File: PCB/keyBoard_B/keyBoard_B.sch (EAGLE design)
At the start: 597 parts, among them IC1 MEGA8-AI, J1 J, J10 J, J11 J, J12 J, J13 J, J14 J, J15 J, J16 J, J17 J, J2 J, J3 J, J4 J, J5 J, J6 J, J7 J, J8 J, J9 J

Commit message: move +m2
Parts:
- removed D100, D101, D102, D103, D104, D105, D106, D107, D108, D109, D110, D87, D88, D89, D90, D91, D92, D93, D94, D95, D96, D97, D98, D99: LL4148, detali:LL4148
- removed HL4: (no value), led:RGB2X5
- removed IC1: MEGA8-AI, atmel:MEGA8-AI
- removed JA100, JA101, JA102, JA103, JA104, JA105, JA106, JA107, JA108, JA109, JA110, JA87, JA88, JA89, JA90, JA91, JA92, JA93, JA94, JA95, JA96, JA97, JA98, JA99, JB100, JB101, JB102, JB103, JB104, JB105, JB106, JB107, JB108, JB109, JB110, JB87, JB88, JB89, JB90, JB91, JB92, JB93, JB94, JB95, JB96, JB97, JB98, JB99: (no value), detali:SJ
- removed S100: 4, cherrymx:CHERRY-MX-4P
- removed S101: 5, cherrymx:CHERRY-MX-4P
- removed S102: 6, cherrymx:CHERRY-MX-4P
- removed S103: +, cherrymx:CHERRY-MX-4P
- removed S104: 1, cherrymx:CHERRY-MX-4P
- removed S105: 2, cherrymx:CHERRY-MX-4P
- removed S106: 3, cherrymx:CHERRY-MX-4P
- removed S107: NumEnter, cherrymx:CHERRY-MX-4P
- removed S107B: NumEnter, cherrymx:CHERRY-MX
- removed S108: 0, cherrymx:CHERRY-MX-4P
- removed S109: 00, cherrymx:CHERRY-MX-4P
- removed S110: ., cherrymx:CHERRY-MX-4P
- removed S67B: |, cherrymx:CHERRY-MX
- removed S74B: Enter, cherrymx:CHERRY-MX
- removed S87: Num, cherrymx:CHERRY-MX-4P
- removed S88: D, cherrymx:CHERRY-MX-4P
- removed S89: E, cherrymx:CHERRY-MX-4P
- removed S90: F, cherrymx:CHERRY-MX-4P
- removed S91: /, cherrymx:CHERRY-MX-4P
- removed S92: A, cherrymx:CHERRY-MX-4P
- removed S93: B, cherrymx:CHERRY-MX-4P
- removed S94: C, cherrymx:CHERRY-MX-4P
- removed S95: *, cherrymx:CHERRY-MX-4P
- removed S96: 7, cherrymx:CHERRY-MX-4P
- removed S97: 8, cherrymx:CHERRY-MX-4P
- removed S98: 9, cherrymx:CHERRY-MX-4P
- removed S99: -, cherrymx:CHERRY-MX-4P
- removed SV2: (no value), con-lsta:FE06-1
- removed SV3: (no value), con-lsta:FE07-1
- added 3D3: 74AC138N, detali2:74AC138N
- added JA67B, JB67B: (no value), detali:SJ
- S47, S48, S49, S50, S51, S52, S53, S54, S55, S56, S57, S58, S59, S60, S61, S62, S63, S64, S65, S66, S67, S67C, S68, S69, S70, S71, S72, S73, S74, S74A, S75, S76, S77, S78, S79, S80, S81, S82, S83, S84, S85, S86: device cherrymx:CHERRY-MX -> cherrymx:CHERRY-MX-4P
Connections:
- removed net 3A1: JA103.2, JA89.2, JA96.2, JA97.2, JA98.2, SV2.1
- removed net 3A2: JA100.2, JA101.2, JA102.2, SV2.2
- removed net 3A3: JA104.2, JA105.2, JA106.2, JA107.2, JA88.2, JA90.2, JA92.2, SV2.3
- removed net 3A4: JA108.2, JA110.2, SV2.4
- removed net 3A5: JA87.2, JA91.2, JA94.2, JA95.2, SV2.5
- removed net 3A6: JA93.2, JA99.2, SV2.6
- removed net 3B0: D92.C, SV3.1
- removed net 3B10: D100.C, D104.C, D87.C, D96.C, SV3.7
- removed net 3B2: D88.C, D89.C, D94.C, SV3.2
- removed net 3B3: D90.C, D93.C, SV3.3
- removed net 3B7: D103.C, D107.C, SV3.4
- removed net 3B8: D102.C, D106.C, D110.C, D95.C, D98.C, D99.C, SV3.5
- removed net 3B9: D101.C, D105.C, D108.C, D91.C, D97.C, SV3.6
- removed net N$269: D88.A, JB88.1
- removed net N$270: JB87.2, S87G$1.PIN-1
- removed net N$271: JB88.2, S88G$1.PIN-1
- removed net N$272: JA87.1, S87G$1.PIN-2
- removed net N$273: JA88.1, S88G$1.PIN-2
- removed net N$274: D89.A, JB89.1
- removed net N$275: JB89.2, S89G$1.PIN-1
- removed net N$276: JA89.1, S89G$1.PIN-2
- removed net N$277: D90.A, JB90.1
- removed net N$278: JB90.2, S90G$1.PIN-1
- removed net N$279: JA90.1, S90G$1.PIN-2
- removed net N$280: D91.A, JB91.1
- removed net N$281: JB91.2, S91G$1.PIN-1
- removed net N$282: JA91.1, S91G$1.PIN-2
- removed net N$283: JB92.2, S92G$1.PIN-1
- removed net N$284: D92.A, JB92.1
- removed net N$285: JA92.1, S92G$1.PIN-2
- removed net N$286: JA93.1, S93G$1.PIN-2
- removed net N$287: JB93.2, S93G$1.PIN-1
- removed net N$288: D93.A, JB93.1
- removed net N$289: D94.A, JB94.1
- removed net N$290: JB94.2, S94G$1.PIN-1
- removed net N$291: JA94.1, S94G$1.PIN-2
- removed net N$292: D95.A, JB95.1
- removed net N$293: JB95.2, S95G$1.PIN-1
- removed net N$294: JA95.1, S95G$1.PIN-2
- removed net N$295: D96.A, JB96.1
- removed net N$296: JB96.2, S96G$1.PIN-1
- removed net N$297: JA96.1, S96G$1.PIN-2
- removed net N$298: JB97.2, S97G$1.PIN-1
- removed net N$299: JA97.1, S97G$1.PIN-2
- removed net N$300: D97.A, JB97.1
- removed net N$301: D98.A, JB98.1
- removed net N$302: JB98.2, S98G$1.PIN-1
- removed net N$303: JA98.1, S98G$1.PIN-2
- removed net N$304: D99.A, JB99.1
- removed net N$305: JB99.2, S99G$1.PIN-1
- removed net N$306: JA99.1, S99G$1.PIN-2
- removed net N$307: D100.A, JB100.1
- removed net N$308: JB100.2, S100G$1.PIN-1
- removed net N$309: JA100.1, S100G$1.PIN-2
- removed net N$310: JB101.2, S101G$1.PIN-1
- removed net N$311: D101.A, JB101.1
- removed net N$312: JA101.1, S101G$1.PIN-2
- removed net N$313: D102.A, JB102.1
- removed net N$314: JB102.2, S102G$1.PIN-1
- removed net N$315: JA102.1, S102G$1.PIN-2
- removed net N$316: D103.A, JB103.1
- removed net N$317: JB103.2, S103G$1.PIN-1
- removed net N$318: JA103.1, S103G$1.PIN-2
- removed net N$319: JB107.2, S107B.PIN-1, S107G$1.PIN-1
- removed net N$320: JB104.2, S104G$1.PIN-1
- removed net N$321: JA104.1, S104G$1.PIN-2
- removed net N$322: JB105.2, S105G$1.PIN-1
- removed net N$323: D105.A, JB105.1
- removed net N$324: JA105.1, S105G$1.PIN-2
- removed net N$325: D106.A, JB106.1
- removed net N$326: JB106.2, S106G$1.PIN-1
- removed net N$327: JA106.1, S106G$1.PIN-2
- removed net N$328: D107.A, JB107.1
- removed net N$329: JB108.2, S108G$1.PIN-1
- removed net N$330: JA108.1, S108G$1.PIN-2
- removed net N$331: D108.A, JB108.1
- removed net N$332: JB109.2, S109G$1.PIN-1
- removed net N$333: D109.A, JB109.1
- removed net N$334: JA109.1, S109G$1.PIN-2
- removed net N$335: D110.A, JB110.1
- removed net N$336: JB110.2, S110G$1.PIN-1
- removed net N$337: JA110.1, S110G$1.PIN-2
- net N$112: now also S47G$1.PIN-1; no longer S47.PIN-1
- net N$127: now also S53G$1.PIN-1; no longer S53.PIN-1
- net N$153: now also S60G$1.PIN-1; no longer S60.PIN-1
- net N$154: now also S68G$1.PIN-1; no longer S68.PIN-1
- net N$155: now also S75G$1.PIN-1; no longer S75.PIN-1
- net N$156: now also S82G$1.PIN-1; no longer S82.PIN-1
- net N$157: now also S48G$1.PIN-1; no longer S48.PIN-1
- net N$158: now also S54G$1.PIN-1; no longer S54.PIN-1
- net N$159: now also S61G$1.PIN-1; no longer S61.PIN-1
- net N$160: now also S69G$1.PIN-1; no longer S69.PIN-1
- net N$161: now also S76G$1.PIN-1; no longer S76.PIN-1
- net N$162: now also S83G$1.PIN-1; no longer S83.PIN-1
- net N$163: now also S49G$1.PIN-1; no longer S49.PIN-1
- net N$164: now also S55G$1.PIN-1; no longer S55.PIN-1
- net N$165: now also S62G$1.PIN-1; no longer S62.PIN-1
- net N$166: now also S70G$1.PIN-1; no longer S70.PIN-1
- net N$167: now also S77G$1.PIN-1; no longer S77.PIN-1
- net N$168: now also S84G$1.PIN-1; no longer S84.PIN-1
- net N$169: now also S50G$1.PIN-1; no longer S50.PIN-1
- net N$170: now also S56G$1.PIN-1; no longer S56.PIN-1
- net N$171: now also S71G$1.PIN-1; no longer S71.PIN-1
- net N$172: now also S78G$1.PIN-1; no longer S78.PIN-1
- net N$173: now also S85G$1.PIN-1; no longer S85.PIN-1
- net N$174: now also S51G$1.PIN-1; no longer S51.PIN-1
- net N$175: now also S57G$1.PIN-1; no longer S57.PIN-1
- net N$176: now also S64G$1.PIN-1; no longer S64.PIN-1
- net N$177: now also S72G$1.PIN-1; no longer S72.PIN-1
- net N$178: now also S79G$1.PIN-1; no longer S79.PIN-1
- net N$179: now also S86G$1.PIN-1; no longer S86.PIN-1
- net N$180: now also S58G$1.PIN-1; no longer S58.PIN-1
- net N$181: now also S65G$1.PIN-1; no longer S65.PIN-1
- net N$182: now also S80G$1.PIN-1; no longer S80.PIN-1
- net N$183: now also S59G$1.PIN-1; no longer S59.PIN-1
- net N$184: now also S66G$1.PIN-1; no longer S66.PIN-1
- net N$185: now also S67G$1.PIN-1; no longer S67.PIN-1, S67B.PIN-1, S67C.PIN-2
- net N$186: now also S81G$1.PIN-1; no longer S81.PIN-1
- net N$224: now also JB67B.1
- net N$227: now also S66G$1.PIN-2; no longer S66.PIN-2
- net N$228: now also S47G$1.PIN-2; no longer S47.PIN-2
- net N$229: now also S53G$1.PIN-2; no longer S53.PIN-2
- net N$230: now also S60G$1.PIN-2; no longer S60.PIN-2
- net N$231: now also S68G$1.PIN-2; no longer S68.PIN-2
- net N$232: now also S75G$1.PIN-2; no longer S75.PIN-2
- net N$233: now also S82G$1.PIN-2; no longer S82.PIN-2
- net N$234: now also S48G$1.PIN-2; no longer S48.PIN-2
- net N$235: now also S54G$1.PIN-2; no longer S54.PIN-2
- net N$236: now also S61G$1.PIN-2; no longer S61.PIN-2
- net N$237: now also S69G$1.PIN-2; no longer S69.PIN-2
- net N$238: now also S76G$1.PIN-2; no longer S76.PIN-2
- net N$239: now also S83G$1.PIN-2; no longer S83.PIN-2
- net N$240: now also S49G$1.PIN-2; no longer S49.PIN-2
- net N$241: now also S55G$1.PIN-2; no longer S55.PIN-2
- net N$242: now also S62G$1.PIN-2; no longer S62.PIN-2
- net N$243: now also S70G$1.PIN-2; no longer S70.PIN-2
- net N$244: now also S77G$1.PIN-2; no longer S77.PIN-2
- net N$245: now also S84G$1.PIN-2; no longer S84.PIN-2
- net N$246: now also S50G$1.PIN-2; no longer S50.PIN-2
- net N$247: now also S56G$1.PIN-2; no longer S56.PIN-2
- net N$248: now also S63G$1.PIN-2; no longer S63.PIN-2
- net N$249: now also S71G$1.PIN-2; no longer S71.PIN-2
- net N$250: now also S78G$1.PIN-2; no longer S78.PIN-2
- net N$251: now also S85G$1.PIN-2; no longer S85.PIN-2
- net N$252: now also S51G$1.PIN-2; no longer S51.PIN-2
- net N$253: now also S57G$1.PIN-2; no longer S57.PIN-2
- net N$254: now also S64G$1.PIN-2; no longer S64.PIN-2
- net N$255: now also S72G$1.PIN-2; no longer S72.PIN-2
- net N$256: now also S79G$1.PIN-2; no longer S79.PIN-2
- net N$257: now also S86G$1.PIN-2; no longer S86.PIN-2
- net N$258: now also S52G$1.PIN-2; no longer S52.PIN-2
- net N$259: now also S58G$1.PIN-2; no longer S58.PIN-2
- net N$260: now also S65G$1.PIN-2; no longer S65.PIN-2
- net N$261: now also S73G$1.PIN-2; no longer S73.PIN-2
- net N$262: now also S80G$1.PIN-2; no longer S80.PIN-2
- net N$263: now also S81G$1.PIN-2; no longer S81.PIN-2
- net N$264: now also S67G$1.PIN-2; no longer S67.PIN-2, S67B.PIN-2, S67C.PIN-1
- net N$265: now also S59G$1.PIN-2; no longer S59.PIN-2
- net N$267: now also S74G$1.PIN-2; no longer S74.PIN-2
- net N$268: now also JA67.2, JA67B.2; no longer D87.A, JB87.1
- net N$51: now also JB67B.2, S67CG$1.PIN-2; no longer JA107.1, S107B.PIN-2, S107G$1.PIN-2
- net N$60: now also JA67B.1, S67CG$1.PIN-1; no longer D104.A, JB104.1
- net N$70: now also S74G$1.PIN-1; no longer S74.PIN-1
- net N$71: now also S52G$1.PIN-1; no longer S52.PIN-1
- net N$84: now also S63G$1.PIN-1; no longer S63.PIN-1
- net N$89: now also S73G$1.PIN-1; no longer S73.PIN-1
- net N$94: now also S74AG$1.PIN-1; no longer S74A.PIN-1, S74B.PIN-1
- net N$97: now also S74AG$1.PIN-2; no longer S74A.PIN-2, S74B.PIN-2
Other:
- moved on the sheet: D67, S67C

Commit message: .
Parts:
- removed 2S1: (no value), con-lsta:FE10-1
- removed 2S2, 2S3: (no value), con-lsta:FE08-1
- removed 2S4: (no value), con-lsta:FE05-1
- removed R3: 1k, rcl:R-EU_R0805
- added S67C1: |, cherrymx:CHERRY-MX-4P
- added U$88: CHERRY-MX, cherrymx:CHERRY-MX
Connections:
- removed net 2A2: 2S3.2, JA47.2, JA60.2
- removed net 2A4: 2S3.4, JA68.2, JA82.2
- removed net 2B0: 2S1.1, D53.C
- removed net 2B1: 2S1.2, D54.C
- removed net 2B10: 2S2.1, D82.C
- removed net 2B4: 2S1.5, D60.C, D61.C, D68.C, D69.C, D75.C, D76.C
- removed net 2B6: 2S1.7, D47.C, D48.C, D83.C
- removed net GND_K2: R3.1
- removed net N$152: R3.2
- net 2A6: no longer 2S3.6, JA75.2
- net 2A7: no longer 2S3.7
- net 2A8: no longer 2S3.8, JA53.2
- net N$94: now also U$88.PIN-1
- net N$97: now also U$88.PIN-2
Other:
- moved on the sheet: D64B, JA59, JA66, JA67, JA67B, JA74B, JB74B, S59, S66, S67, S67C, S74

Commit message: arc
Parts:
- added IC1: 74ALS04N, detali2:74ALS04N
- added S67C2: FN1, cherrymx:CHERRY-MX-4P
- S67C1: value | -> FN2
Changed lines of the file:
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@@
 <part name="JB67B" library="detali" deviceset="SJ" device=""/>
 <part name="U$88" library="cherrymx" deviceset="CHERRY-MX" device=""/>
-<part name="S67C1" library="cherrymx" deviceset="CHERRY-MX-4P" device="" value="|"/>
+<part name="S67C1" library="cherrymx" deviceset="CHERRY-MX-4P" device="" value="FN2"/>
+<part name="IC1" library="detali2" deviceset="74*04" device="N" technology="ALS"/>
+<part name="S67C2" library="cherrymx" deviceset="CHERRY-MX-4P" device="" value="FN1"/>
 </parts>
 <sheets>
@@
 <instance part="U$88" gate="G$1" x="480.06" y="-7.62"/>
 <instance part="S67C1" gate="G$1" x="414.02" y="-2.54" rot="MR0"/>
+<instance part="IC1" gate="A" x="322.58" y="-73.66"/>
+<instance part="S67C2" gate="G$1" x="363.22" y="-5.08" rot="MR0"/>
 </instances>
 <busses>

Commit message: get all vil
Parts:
- removed 1S1, 1S1O: (no value), con-lsta:FE10-1
- removed 1S2, 1S2O, 1S3, 1S3O: (no value), con-lsta:FE08-1
- removed 1S4, 1S4O: (no value), con-lsta:FE05-1
- removed 3D1: 74HC138N, detali:74HC138N
- removed 3D2: К155ЛА4, detali:74HC10N
- removed 3D3: 74AC138N, detali2:74AC138N
- removed D10, D11, D111, D112, D113, D114, D115, D116, D117, D118, D119, D12, D120, D121, D122, D123, D124, D125, D126, D127, D128, D129, D13, D130, D131, D132, D133, D134, D135, D136, D14, D15, D16, D17, D18, D19, D20, D21, D22, D23, D24, D25, D26, D27, D28, D29, D3, D30, D31, D32, D33, D34, D35, D36, D37, D38, D39, D4, D40, D41, D42, D43, D44, D45, D46, D5, D6, D7, D8, D9: LL4148, detali:LL4148
- removed HL1, HL2, HL3: (no value), led:RGB2X5
- removed IC1: 74ALS04N, detali2:74ALS04N
- removed J13: J, detali:J
- removed JA1, JA10, JA11, JA12, JA2, JA3, JA4, JA5, JA6, JA7, JA8, JA9, JB10, JB11, JB12, JB13, JB14, JB15, JB16, JB17, JB2, JB4, JB5, JB6, JB7, JB8, JB9: (no value), jumper:SJ
- removed JA111, JA112, JA113, JA114, JA115, JA116, JA117, JA118, JA119, JA120, JA121, JA122, JA123, JA124, JA125, JA126, JA127, JA128, JA129, JA13, JA130, JA131, JA132, JA133, JA14, JA15, JA16, JA17, JA18, JA19, JA20, JA21, JA22, JA23, JA24, JA25, JA26, JA27, JA28, JA29, JA30, JA31, JA32, JA33, JA34, JA35, JA36, JA37, JA38, JA39, JA40, JA41, JA42, JA43, JA44, JA45, JA46, JB1, JB111, JB112, JB113, JB114, JB115, JB116, JB117, JB118, JB119, JB120, JB121, JB122, JB123, JB124, JB125, JB126, JB127, JB128, JB129, JB130, JB131, JB132, JB133, JB18, JB19, JB20, JB21, JB22, JB23, JB24, JB25, JB26, JB27, JB28, JB29, JB3, JB30, JB31, JB32, JB33, JB34, JB35, JB36, JB37, JB38, JB39, JB40, JB41, JB42, JB43, JB44, JB45, JB46, JB67B: (no value), detali:SJ
- removed LED1: (no value), detali:LED5MM
- removed R1, R2: 1k, rcl:R-EU_R1206W
- removed R4, R5, R6: 10k, rcl:R-EU_R1206W
- removed R7, R8: (no value), rcl:R-EU_R1206W
- removed S1: Scroll Lock, cherrymx:CHERRY-MX-LED
- removed S10: Left, cherrymx:CHERRY-MX
- removed S107B1, S130: NumEnter, cherrymx:CHERRY-MX-4P
- removed S11: Down, cherrymx:CHERRY-MX
- removed S111: D, cherrymx:CHERRY-MX-4P
- removed S112: E, cherrymx:CHERRY-MX-4P
- removed S113: F, cherrymx:CHERRY-MX-4P
- removed S114: /, cherrymx:CHERRY-MX-4P
- removed S115: A, cherrymx:CHERRY-MX-4P
- removed S116: B, cherrymx:CHERRY-MX-4P
- removed S117: C, cherrymx:CHERRY-MX-4P
- removed S118: *, cherrymx:CHERRY-MX-4P
- removed S119: 7, cherrymx:CHERRY-MX-4P
- removed S12: Right, cherrymx:CHERRY-MX
- removed S120: 8, cherrymx:CHERRY-MX-4P
- removed S121: 9, cherrymx:CHERRY-MX-4P
- removed S122: -, cherrymx:CHERRY-MX-4P
- removed S123: 4, cherrymx:CHERRY-MX-4P
- removed S124: 5, cherrymx:CHERRY-MX-4P
- removed S125: 6, cherrymx:CHERRY-MX-4P
- removed S126: +, cherrymx:CHERRY-MX-4P
- removed S127: 1, cherrymx:CHERRY-MX-4P
- removed S128: 2, cherrymx:CHERRY-MX-4P
- removed S129: 3, cherrymx:CHERRY-MX-4P
- removed S13: F1, cherrymx:CHERRY-MX
- removed S131: 0, cherrymx:CHERRY-MX-4P
- removed S132: 00, cherrymx:CHERRY-MX-4P
- removed S133: ., cherrymx:CHERRY-MX-4P
- removed S134: NumLock, detali:31-XX
- removed S14: F2, cherrymx:CHERRY-MX
- removed S15: F3, cherrymx:CHERRY-MX
- removed S16: F4, cherrymx:CHERRY-MX
- removed S17: F5, cherrymx:CHERRY-MX
- removed S18: F6, cherrymx:CHERRY-MX
- removed S19: 1, cherrymx:CHERRY-MX
- removed S2: ESC, cherrymx:CHERRY-MX-LED
- removed S20: 2, cherrymx:CHERRY-MX
- removed S21: 3, cherrymx:CHERRY-MX
- removed S22: 4, cherrymx:CHERRY-MX
- removed S23: 5, cherrymx:CHERRY-MX
- removed S24: 6, cherrymx:CHERRY-MX
- removed S25: TAB, cherrymx:CHERRY-MX
- removed S26: Q, cherrymx:CHERRY-MX
- removed S27: W, cherrymx:CHERRY_MX
- removed S28: E, cherrymx:CHERRY-MX
- removed S29: R, cherrymx:CHERRY-MX
- removed S3: Ins, cherrymx:CHERRY-MX-LED
- removed S30: T, cherrymx:CHERRY-MX
- removed S31: LCtrl, cherrymx:CHERRY-MX
- removed S32: A, cherrymx:CHERRY-MX
- removed S33: S, cherrymx:CHERRY-MX
- removed S34: D, cherrymx:CHERRY-MX
- removed S35: F, cherrymx:CHERRY-MX
- removed S36: G, cherrymx:CHERRY-MX
- removed S37, S37B, S37B1: L Shift, cherrymx:CHERRY-MX
- removed S38: Z, cherrymx:CHERRY-MX
- removed S39: X, cherrymx:CHERRY-MX
- removed S4: Pause, cherrymx:CHERRY_MX
- removed S40: C, cherrymx:CHERRY-MX
- removed S41: V, cherrymx:CHERRY-MX
- removed S42: B, cherrymx:CHERRY-MX
- removed S43: Caps Lock, cherrymx:CHERRY-MX-LED
- removed S44: Alt, cherrymx:CHERRY-MX
- removed S45: Menu(Win), cherrymx:CHERRY-MX
- removed S46: Space, cherrymx:CHERRY-MX
- removed S5: Home, cherrymx:CHERRY-MX
- removed S6: P Up, cherrymx:CHERRY-MX
- removed S67C2: FN1, cherrymx:CHERRY-MX-4P
- removed S7: End, cherrymx:CHERRY-MX
- removed S8: P Dn, cherrymx:CHERRY-MX
- removed S9: Up, cherrymx:CHERRY-MX
- removed U$88: CHERRY-MX, cherrymx:CHERRY-MX
- added 2D1: 74HC138N, detali2:74AC138N
- added 2D2: 74HC04N, detali2:74ALS04N
- added D67B, D87: LL4148, detali:LL4148
- added J18, J19, J21, J22, J23, J24, J25, J26, J27, J28, J29, J30, J31, J32, J33, J34, J35, J36, J37, J38, J39, J40, J41, J42, J43, J44, J46, J48, J49, J50, J51, J52, J53: J, detali2:J
- added JA67B1, JA87, JB67B1, JB87: (no value), detali:SJ
- added R3: 1k, rcl:R-EU_R0805
- added S67B: |u, cherrymx:CHERRY-MX
- added S74B: Enter, cherrymx:CHERRY-MX
- C1: value (none) -> 100n; device rcl:C-EUC1206 -> rcl:C-EUC0805
- C2: value (none) -> 100n
- J1, J10, J11, J12, J14, J15, J16, J17, J2, J3, J4, J5, J6, J7, J8, J9: device detali:J -> detali2:J
- S67: value | -> |d
- S83: value Mouse2(Menu) -> FN3
- S84: value Alt -> R_Alt
- SV1: value (none) -> CON_KB_B; device detali:FE09-1 -> detali2:FE12-1
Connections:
- removed net +5V_K1: 1S4.4, R1.1, R2.1
- removed net 2A1: JA61.2
- removed net 2A3: JA69.2
- removed net 2A5: JA76.2
- removed net 2A6: JA83.2
- removed net 2A7: JA48.2
- removed net 2A8: JA54.2
- removed net A1: 1S3.1, JA1.2, JA26.2, JA28.2, JA29.2
- removed net A2: 1S3.2, 1S3O.2, JA15.2, JA25.2, JA30.2, JA37.2, JA43.2, JA45.2
- removed net A3: 1S3.3, JA27.2, JA32.2, JA33.2, JA34.2, JA35.2
- removed net A4: 1S3.4, JA16.2, JA18.2, JA2.2, JA36.2, JA44.2, JA46.2, JA9.2
- removed net A5: 1S3.5, JA38.2, JA39.2, JA40.2, JA41.2
- removed net A6: 1S3.6, JA10.2, JA11.2, JA12.2, JA42.2
- removed net A7: 1S3.7, D24.A, JA13.2, JA14.2, JA23.2, JA3.2, JA31.2, JA5.2, JA6.2
- removed net A8: 1S3.8, JA17.2, JA19.2, JA20.2, JA21.2, JA22.2, JA4.2, JA7.2, JA8.2
- removed net B0: 1S1.1, D2.C, D25.C, D26.C, D32.C, D38.C
- removed net B1: 1S1.2, D13.C, D33.C, D39.C, D43.C, HL1.AB, HL2.AB
- removed net B10: 1S2.1, D11.C, D46.C
- removed net B11: 1S2.2, D37.C
- removed net B12: 1S2.3
- removed net B13: 1S2.4, D22.C
- removed net B14: 1S2.5, D1.C, D27.C, D4.C, D44.C
- removed net B15: 1S2.6, D17.C, D31.C
- removed net B16: 1S2.7, D45.C
- removed net B17: 1S2.8
- removed net B2: 1S1.3, D14.C, D15.C, D16.C, D28.C, D34.C, D40.C, HL3.AB
- removed net B3: 1S1.4, D23.C, D29.C, D30.C, D35.C, D36.C, D41.C, D42.C
- removed net B4: 1S1.5, D19.C, JA24.2
- removed net B5: 1S1.6, D18.C, D20.C
- removed net B6: 1S1.7, 1S2O.5, D21.C
- removed net B7: 1S1.8, D10.C, D5.C, D7.C, D9.C
- removed net B8: 1S1.9, D6.C, D8.C
- removed net B9: 1S1.10, D12.C, D3.C
- removed net COLN1: 3D2A.O, SV1.2
- removed net COLN2: 3D2B.O, J15.P$1
- removed net COLN3: 3D2C.O, SV1.3
- removed net GND_K1: 1S4.5
- removed net K1: HL1.C, HL3.C
- removed net LED_CAPS: 1S4.3, S43_LED.LED2
- removed net LED_NUM: 1S4.1
- removed net LED_SCR: 1S4.2, S1_LED.LED2
- removed net N$100: JA30.1, S30.PIN-2
- removed net N$101: JA31.1, S31.PIN-2
- removed net N$102: JA32.1, S32.PIN-2
- removed net N$103: JA33.1, S33.PIN-2
- removed net N$104: JA34.1, S34.PIN-2
- removed net N$105: JA35.1, S35.PIN-2
- removed net N$106: JA36.1, S36.PIN-2
- removed net N$107: JA37.1, S37.PIN-2, S37B.PIN-2, S37B1.PIN-2
- removed net N$108: JA38.1, S38.PIN-2
- removed net N$109: JA39.1, S39.PIN-2
- removed net N$110: JA40.1, S40.PIN-2
- removed net N$111: JA41.1, S41.PIN-2
- removed net N$113: JA43.1, S43G$1.PIN-2
- removed net N$114: JA45.1, S45.PIN-2
- removed net N$115: JA46.1, S46.PIN-2
- removed net N$116: JA19.1, S19.PIN-2
- removed net N$117: JA44.1, S44.PIN-2
- removed net N$118: JA21.1, S21.PIN-2
- removed net N$119: JA16.1, S16.PIN-2
- removed net N$120: D17.A, JB17.1
- removed net N$121: D18.A, JB18.1
- removed net N$122: D19.A, JB19.1
- removed net N$123: D20.A, JB20.1
- removed net N$124: D21.A, JB21.1
- removed net N$125: D22.A, JB22.1
- removed net N$126: D23.A, JB23.1
- removed net N$128: D25.A, JB25.1
- removed net N$129: D26.A, JB26.1
- removed net N$130: D27.A, JB27.1
- removed net N$131: D28.A, JB28.1
- removed net N$132: D29.A, JB29.1
- removed net N$133: D30.A, JB30.1
- removed net N$134: D31.A, JB31.1
- removed net N$135: D32.A, JB32.1
- removed net N$136: D33.A, JB33.1
- removed net N$137: D34.A, JB34.1
- removed net N$138: D35.A, JB35.1
- removed net N$139: D36.A, JB36.1
- removed net N$140: D37.A, JB37.1
- removed net N$141: D38.A, JB38.1
- removed net N$142: D39.A, JB39.1
- removed net N$143: D40.A, JB40.1
- removed net N$144: D41.A, JB41.1
- removed net N$145: D42.A, JB42.1
- removed net N$146: D43.A, JB43.1
- removed net N$147: D44.A, JB44.1
- removed net N$148: D45.A, JB45.1
- removed net N$149: D46.A, JB46.1
- removed net N$150: R1.2, S1_LED.LED1
- removed net N$151: R2.2, S43_LED.LED1
- removed net N$28 (its old number): JA10.1, S10.PIN-2
- removed net N$29 (its old number): JA1.1, S1G$1.PIN-2
- removed net N$30: D9.A, JB9.1
- removed net N$31: D11.A, JB11.1
- removed net N$338: D112.A, S134.P
- removed net N$339: JA111.1, S111G$1.PIN-2
- removed net N$340: D113.A, JB112.1
- removed net N$341: JB112.2, S112G$1.PIN-1
- removed net N$342: JA112.1, S112G$1.PIN-2
- removed net N$343: D111.A, JB111.1
- removed net N$344: JB111.2, S111G$1.PIN-1
- removed net N$345: D114.A, JB113.1
- removed net N$346: JB113.2, S113G$1.PIN-1
- removed net N$347: JA113.1, S113G$1.PIN-2
- removed net N$348: D115.A, JB114.1
- removed net N$349: JB114.2, S114G$1.PIN-1
- removed net N$350: JA114.1, S114G$1.PIN-2
- removed net N$351: JB115.2, S115G$1.PIN-1
- removed net N$352: D116.A, JB115.1
- removed net N$353: JA115.1, S115G$1.PIN-2
- removed net N$354: JA116.1, S116G$1.PIN-2
- removed net N$355: JB116.2, S116G$1.PIN-1
- removed net N$356: D117.A, JB116.1
- removed net N$357: D118.A, JB117.1
- removed net N$358: JB117.2, S117G$1.PIN-1
- removed net N$359: JA117.1, S117G$1.PIN-2
- removed net N$360: D119.A, JB118.1
- removed net N$361: JB118.2, S118G$1.PIN-1
- removed net N$362: JA118.1, S118G$1.PIN-2
- removed net N$363: D120.A, JB119.1
- removed net N$364: JB119.2, S119G$1.PIN-1
- removed net N$365: JA119.1, S119G$1.PIN-2
- removed net N$366: JB120.2, S120G$1.PIN-1
- removed net N$367: JA120.1, S120G$1.PIN-2
- removed net N$368: D121.A, JB120.1
- removed net N$369: D122.A, JB121.1
- removed net N$370: JB121.2, S121G$1.PIN-1
- removed net N$371: JA121.1, S121G$1.PIN-2
- removed net N$372: D123.A, JB122.1
- removed net N$373: JB122.2, S122G$1.PIN-1
- removed net N$374: JA122.1, S122G$1.PIN-2
- removed net N$375: D124.A, JB123.1
- removed net N$376: JB123.2, S123G$1.PIN-1
- removed net N$377: JA123.1, S123G$1.PIN-2
- removed net N$378: JB124.2, S124G$1.PIN-1
- removed net N$379: D125.A, JB124.1
- removed net N$38: JA14.1, S14.PIN-2
- removed net N$380: JA124.1, S124G$1.PIN-2
- removed net N$381: D126.A, JB125.1
- removed net N$382: JB125.2, S125G$1.PIN-1
- removed net N$383: JA125.1, S125G$1.PIN-2
- removed net N$384: D127.A, JB126.1
- removed net N$385: JB126.2, S126G$1.PIN-1
- removed net N$386: JA126.1, S126G$1.PIN-2
- removed net N$387: JB130.2, S107B1G$1.PIN-1, S130G$1.PIN-1
- removed net N$388: JA130.1, S107B1G$1.PIN-2, S130G$1.PIN-2
- removed net N$389: D128.A, JB127.1
- removed net N$390: JB127.2, S127G$1.PIN-1
- removed net N$391: JA127.1, S127G$1.PIN-2
- removed net N$392: JB128.2, S128G$1.PIN-1
- removed net N$393: D129.A, JB128.1
- removed net N$394: JA128.1, S128G$1.PIN-2
- removed net N$395: D130.A, JB129.1
- removed net N$396: JB129.2, S129G$1.PIN-1
- removed net N$397: JA129.1, S129G$1.PIN-2
- removed net N$398: JB131.2, S131G$1.PIN-1
- removed net N$399: JA131.1, S131G$1.PIN-2
- removed net N$40: JA13.1, S13.PIN-2
- removed net N$400: D132.A, JB131.1
- removed net N$401: JB132.2, S132G$1.PIN-1
- removed net N$402: D133.A, JB132.1
- removed net N$403: JA132.1, S132G$1.PIN-2
- removed net N$404: D134.A, JB133.1
- removed net N$405: JB133.2, S133G$1.PIN-1
- removed net N$406: JA133.1, S133G$1.PIN-2
- removed net N$407: 3D2B.I0, 3D2B.I1, 3D2B.I2, JA112.2, JA116.2, JA120.2, JA124.2, JA125.2, JA128.2, JA129.2, JA133.2, R5.1
- removed net N$408: D111.C, D117.C, D118.C, J9.P$2
- removed net N$409: D123.C, D126.C, D128.C, J4.P$1
- removed net N$41: D14.A, JB14.1
- removed net N$410: 3D2A.I0, 3D2A.I1, 3D2A.I2, JA111.2, JA115.2, JA119.2, JA123.2, JA127.2, JA131.2, JA132.2, R4.1, S134.S
- removed net N$411: 3D1A.Y5, D112.C, D113.C, D114.C
- removed net N$412: 3D1A.Y4, D115.C, J7.P$2
- removed net N$413: 3D1A.Y3, D119.C, J3.P$2
- removed net N$414: 3D1A.Y1, D127.C, D130.C, D132.C
- removed net N$415: D116.C, D121.C, D122.C, J11.P$2
- removed net N$416: D131.A, J8.P$2, JA113.2, JA114.2, JA117.2, JA118.2, JA121.2, JA122.2, JA126.2
- removed net N$417: D131.C, JB130.1
- removed net N$418: D124.C, D129.C, J2.P$1
- removed net N$419: J1.P$1, J2.P$2
- removed net N$42: JB42.2, S42.PIN-2
- removed net N$420: J1.P$2, J3.P$1
- removed net N$421: 3D1A.Y2, J4.P$2
- removed net N$422: D120.C, D125.C, J5.P$1
- removed net N$423: J6.P$2, J7.P$1
- removed net N$424: J5.P$2, J6.P$1
- removed net N$425: 3D2C.I0, 3D2C.I1, 3D2C.I2, J14.P$1, R6.1
- removed net N$426: 3D1A.Y7, J10.P$1
- removed net N$427: J10.P$2, J9.P$1
- removed net N$428: J11.P$1, J12.P$1
- removed net N$429: J12.P$2, J13.P$1
- removed net N$43: JA42.1, S42.PIN-1
- removed net N$430: 3D1A.Y6, J13.P$2
- removed net N$431: 3D1A.G1, R7.2
- removed net N$432: 3D1A.A, SV1.8
- removed net N$433: 3D1A.B, SV1.7
- removed net N$434: 3D1A.C, SV1.6
- removed net N$435: LED1.A, R8.2
- removed net N$436: J14.P$2, J8.P$1
- removed net N$437: J15.P$2, J16.P$1
- removed net N$438: J16.P$2, SV1.5
- removed net N$439: J17.P$2, SV1.4
- removed net N$44: JB27.2, S27.PIN-1
- removed net N$440: J17.P$1, R8.1
- removed net N$441: D135.A, D136.C
- removed net N$442: 3D2P.VCC, C2.1, D135.C
- removed net N$45: JA27.1, S27.PIN-2
- removed net N$46: JB17.2, S17.PIN-2
- removed net N$47: JA17.1, S17.PIN-1
- removed net N$48: D24.C, JB24.1
- removed net N$49: JB24.2, S24.PIN-2
- removed net N$50: JA24.1, S24.PIN-1
- removed net N$51 (its old number): JB67B.2, S67CG$1.PIN-2
- removed net N$52: D4.A, JB4.1
- removed net N$53: D6.A, JB6.1
- removed net N$54: D8.A, JB8.1
- removed net N$56: D12.A, JB12.1
- removed net N$57: D13.A, JB13.1
- removed net N$58: JB19.2, S19.PIN-1
- removed net N$59: JB25.2, S25.PIN-1
- removed net N$61: JB31.2, S31.PIN-1
- removed net N$62: JB37.2, S37.PIN-1, S37B.PIN-1, S37B1.PIN-1
- removed net N$63: JB43.2, S43G$1.PIN-1
- removed net N$64: JB26.2, S26.PIN-1
- removed net N$65: JB44.2, S44.PIN-1
- removed net N$66: JB18.2, S18.PIN-1
- removed net N$68: JB30.2, S30.PIN-1
- removed net N$69: JB36.2, S36.PIN-1
- removed net N$72: JB23.2, S23.PIN-1
- removed net N$73: JB29.2, S29.PIN-1
- removed net N$74: JB35.2, S35.PIN-1
- removed net N$75: JB41.2, S41.PIN-1
- removed net N$76: JB16.2, S16.PIN-1
- removed net N$77: JB22.2, S22.PIN-1
- removed net N$78: JB28.2, S28.PIN-1
- removed net N$79: JB34.2, S34.PIN-1
- removed net N$80: JB40.2, S40.PIN-1
- removed net N$81: JB46.2, S46.PIN-1
- removed net N$82: JB15.2, S15.PIN-1
- removed net N$83: JB21.2, S21.PIN-1
- removed net N$85: JB33.2, S33.PIN-1
- removed net N$86: JB39.2, S39.PIN-1
- removed net N$87: JB45.2, S45.PIN-1
- removed net N$88: JA15.1, S15.PIN-2
- removed net N$9: JB6.2, S6.PIN-1
- removed net N$90: JA18.1, S18.PIN-2
- removed net N$91: JA20.1, S20.PIN-2
- removed net N$92: JA22.1, S22.PIN-2
- removed net N$93: JA23.1, S23.PIN-2
- removed net N$95: JA25.1, S25.PIN-2
- removed net N$96: JA26.1, S26.PIN-2
- removed net N$98: JA28.1, S28.PIN-2
- removed net N$99: JA29.1, S29.PIN-2
- removed net R1: HL1.AR, HL2.AR
- removed net R2: HL3.AR
- removed net SCK: 3D1A.Y0, D133.C, D134.C, JA130.2
- new net +3VD: 2D2P.VCC, C2.1, D1.C
- new net 1: D49.C, D50.C, D52.C, D56.C, D64B.C, J44.P$1
- new net 2: D51.C, D58.C, D59.C, J10.P$2, J2.P$2
- new net 2I: 2D1A.Y1, D48.C, J7.P$1
- new net 2J: D55.C, J10.P$1
- new net 3: D47.C, D54.C, D57.C, D63.C, J3.P$2
- new net 3J: D66.C, D67B.C, J4.P$1, J46.P$1
- new net 4: D65.C, D74.C, J5.P$1, J50.P$1
- new net 4J: D64.C, D71.C, J11.P$2, J5.P$2
- new net 4J2: D53.C, D61.C, J11.P$1
- new net 5: D67.C, D73.C, J48.P$1, J6.P$1
- new net 5J: D60.C, D62.C, D69.C, D72.C, J6.P$2
- new net 6: D79.C, D80.C, D81.C, J12.P$2, J53.P$1
- new net 6J2: D70.C, J12.P$1, J14.P$2
- new net 6J3: D68.C, J14.P$1
- new net 7: 2D1A.Y2, D84.C, D85.C, J9.P$1
- new net 7J: D75.C, D76.C, D78.C, J9.P$2
- new net 8: 2D1A.Y3, D86.C, J8.P$2
- new net 8J: D77.C, D82.C, D83.C, D87.C, J8.P$1
- new net D1: J29.P$2, SV1.10
- new net D2: J30.P$2, SV1.9
- new net D3: J31.P$2, SV1.8
- new net G3: J15.P$2, JA62.2, JA63.2, JA71.2
- new net G4: J34.P$2, JA50.2, JA51.2, JA57.2, JA64.2, JA72.2, JA78.2, JA79.2, JA87.2
- new net G5: J21.P$2, JA52.2, JA58.2, JA65.2, JA66.2, JA73.2, JA80.2, JA83.2, JA84.2
- new net G6: J17.P$2, JA59.2, JA67.2, JA67B.2, JA67B1.2, JA74B.2, JA81.2, JA85.2, JA86.2, JB74.1
- new net N$152: J17.P$1, J18.P$2
- new net N$269: J3.P$1, J4.P$2
- new net N$270: 2D2A.O, SV1.5
- new net N$271: JB67B1.2, S67B.PIN-1, S67CG$1.PIN-2
- new net N$275: 2D2F.O, J23.P$2
- new net N$277: 2D1A.G1, R3.2
- new net N$281: 2D2D.O, J28.P$2
- new net N$282: D67B.A, JB67B1.1
- new net N$285: J15.P$1, J16.P$2
- new net N$286: JA87.1, S67C1G$1.PIN-1
- new net N$287: JB87.2, S67C1G$1.PIN-2
- new net N$288: D87.A, JB87.1
- new net N$289: 2D2B.I, J16.P$1
- new net N$290: 2D2F.I, J18.P$1
- new net N$293: J19.P$2, J21.P$1
- new net N$294: 2D2E.I, J19.P$1
- new net N$60: JA67B1.1, S67B.PIN-2
- new net N$67: 2D2C.O, SV1.7
- net +5V: now also 2D1P.VCC, D2.A, R3.1, SV1.11; no longer 3D1P.VCC, D136.A, R4.2, R5.2, R6.2, R7.1, SV1.9
- net G1: now also 2D2D.I, JA47.2, JA48.2, JA49.2, JA53.2, JA60.2, JA68.2, JA75.2, JA82.2; no longer HL1.AG, HL2.AG
- net G2: now also J22.P$2, JA54.2, JA55.2, JA56.2, JA61.2, JA69.2, JA70.2, JA76.2, JA77.2; no longer HL3.AG
- net GND: now also 2D1A.G2A, 2D1A.G2B, 2D1P.GND, 2D2P.GND; no longer 3D1A.G2A, 3D1A.G2B, 3D1P.GND, 3D2P.GND, LED1.C
- net N$1: now also 2D2A.I, J22.P$1; no longer D15.A, JB15.1
- net N$10: now also D1.A, D2.C; no longer JA6.1, S6.PIN-2
- net N$11: now also J1.P$2, J29.P$1; no longer JA8.1, S8.PIN-2
- net N$12: now also J30.P$1, J32.P$2; no longer JB8.2, S8.PIN-1
- net N$13: now also J31.P$1, J33.P$2; no longer JB10.2, S10.PIN-1
- net N$14: now also J1.P$1, J35.P$2; no longer JB1.2, S1G$1.PIN-1
- net N$15: now also J32.P$1, J36.P$2; no longer D2.A, JB2.1
- net N$16: now also J33.P$1, J37.P$2; no longer JB2.2, S2G$1.PIN-2
- net N$161: now also S76G$1.PIN-2; no longer S76G$1.PIN-1
- net N$162: now also S83G$1.PIN-2; no longer S83G$1.PIN-1
- net N$165: now also S62G$1.PIN-2; no longer S62G$1.PIN-1
- net N$168: now also JA73.1, S73G$1.PIN-1; no longer JB84.2, S84G$1.PIN-1
- net N$169: now also S50G$1.PIN-2; no longer S50G$1.PIN-1
- net N$17: now also 2D2C.I, J34.P$1; no longer JA2.1, S2G$1.PIN-1
- net N$172: now also S78G$1.PIN-2; no longer S78G$1.PIN-1
- net N$173: now also S85G$1.PIN-2; no longer S85G$1.PIN-1
- net N$175: now also S57G$1.PIN-2; no longer S57G$1.PIN-1
- net N$176: now also JA57.1, S57G$1.PIN-1; no longer JB64.2, S64G$1.PIN-1
- net N$177: now also JA64.1, S64G$1.PIN-1; no longer JB72.2, S72G$1.PIN-1
- net N$178: now also S79G$1.PIN-2; no longer S79G$1.PIN-1
- net N$18: now also J37.P$1, J38.P$2; no longer D16.A, JB16.1
- net N$180: now also S58G$1.PIN-2; no longer S58G$1.PIN-1
- net N$181: now also S65G$1.PIN-2; no longer S65G$1.PIN-1
- net N$182: now also JA80.1; no longer JB80.2
- net N$183: now also S59G$1.PIN-2; no longer S59G$1.PIN-1
- net N$185: now also S67G$1.PIN-2; no longer S67G$1.PIN-1
- net N$186: now also S81G$1.PIN-2; no longer S81G$1.PIN-1
- net N$19: now also J36.P$1, J40.P$2; no longer JB3.2, S3G$1.PIN-1
- net N$2: now also J23.P$1, SV1.4; no longer JB4.2, S4.PIN-1
- net N$20: now also J35.P$1, J39.P$2; no longer JB5.2, S5.PIN-1
- net N$21: now also J38.P$1, J41.P$2; no longer JB7.2, S7.PIN-1
- net N$22: now also J40.P$1, J42.P$2; no longer JB9.2, S9.PIN-1
- net N$224: no longer JB67B.1
- net N$225: now also JA74.2; no longer JB74.1
- net N$23: now also J39.P$1, J43.P$2; no longer JB11.2, S11.PIN-1
- net N$238: now also S76G$1.PIN-1; no longer S76G$1.PIN-2
- net N$239: now also S83G$1.PIN-1; no longer S83G$1.PIN-2
- net N$24: now also 2D1A.A, J41.P$1; no longer D3.A, JB3.1
- net N$242: now also S62G$1.PIN-1; no longer S62G$1.PIN-2
- net N$245: now also JB80.2, S80G$1.PIN-2; no longer JA84.1, S84G$1.PIN-2
- net N$246: now also S50G$1.PIN-1; no longer S50G$1.PIN-2
- net N$25: now also 2D1A.B, J42.P$1; no longer JB12.2, S12.PIN-1
- net N$250: now also S78G$1.PIN-1; no longer S78G$1.PIN-2
- net N$251: now also S85G$1.PIN-1; no longer S85G$1.PIN-2
- net N$253: now also JB64.2, S64G$1.PIN-2; no longer JA57.1, S57G$1.PIN-2
- net N$254: now also JB72.2, S72G$1.PIN-2; no longer JA64.1, S64G$1.PIN-2
- net N$255: now also S72G$1.PIN-1; no longer S72G$1.PIN-2
- net N$256: now also S79G$1.PIN-1; no longer S79G$1.PIN-2
- net N$259: now also JA65.1, S65G$1.PIN-1; no longer JA58.1, S58G$1.PIN-2
- net N$26: now also 2D1A.C, J43.P$1; no longer D5.A, JB5.1
- net N$260: now also JA58.1, S58G$1.PIN-1; no longer JA65.1, S65G$1.PIN-2
- net N$261: now also JB84.2, S84G$1.PIN-2; no longer JA73.1, S73G$1.PIN-2
- net N$262: now also JA84.1, S84G$1.PIN-1; no longer JA80.1, S80G$1.PIN-2
- net N$263: now also S81G$1.PIN-1; no longer S81G$1.PIN-2
- net N$264: now also S67G$1.PIN-1; no longer S67G$1.PIN-2
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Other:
- note added: "d1"
- note added: "d2"
- note added: "d3"
- note added: "gnd"
- note added: "kbb1"
- note added: "kbb2"
- note added: "kbb3"
- note added: "kbb4"
- note added: "kbb5"
- note added: "kbb6"
- note added: "vcc"

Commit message: fix b
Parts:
- added R1, R2, R4, R6, R7: 10k, rcl:R-EU_R0805
- added R5: 10k, rcl:R-EU_R1206W
- renumbered S67C1 to S87
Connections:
- net N$293 renamed PG5
- removed net N$17: 2D2C.I, J34.P$1
- removed net N$289: 2D2B.I, J16.P$1
- removed net N$290: 2D2F.I, J18.P$1
- removed net N$294: 2D2E.I, J19.P$1
- new net GG5: 2D2E.I, J19.P$1, R6.2
- new net PG3: 2D2B.I, J16.P$1, R4.2
- new net PG4: 2D2C.I, J34.P$1, R5.2
- new net PG6: 2D2F.I, J18.P$1, R7.2
- net +5V: now also R1.1, R2.1, R4.1, R5.1, R6.1, R7.1
- net G1: now also R1.2
- net G2: now also R2.2
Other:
- moved on the sheet: 2D1P, 2D2P, C1, C2, D1, D2

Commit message: .
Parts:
- removed JB67B1: (no value), detali:SJ
- added J13: J, detali2:J
- added JB67B: (no value), detali:SJ
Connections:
- new net N$17: J13.P$2, JB67B.2
- net N$271: now also J13.P$1; no longer JB67B1.2
- net N$282: now also JB67B.1; no longer JB67B1.1
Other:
- moved on the sheet: D67B

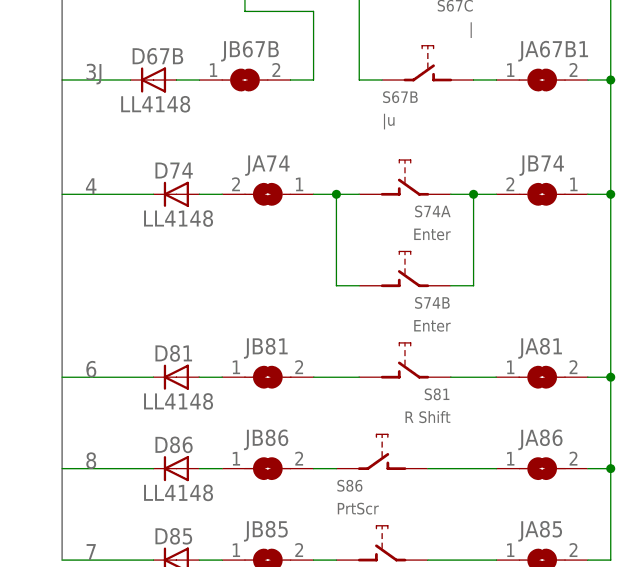
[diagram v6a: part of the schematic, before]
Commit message: add kesize table. bad pcb a b
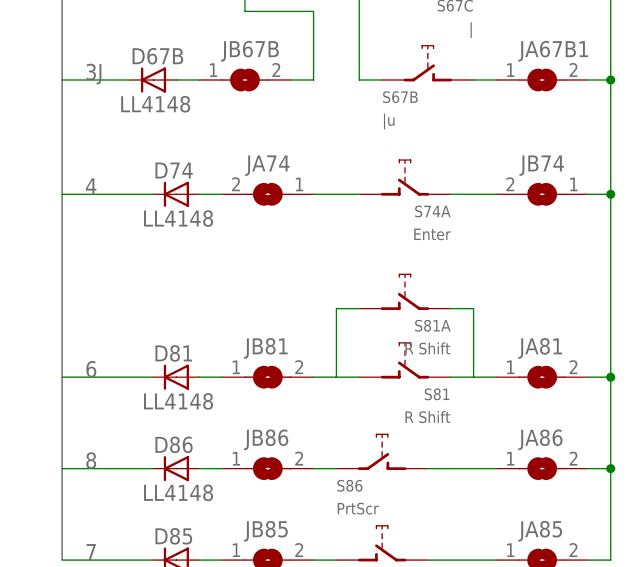
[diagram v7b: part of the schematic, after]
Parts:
- removed S74B: Enter, cherrymx:CHERRY-MX
- added S81A: R Shift, cherrymx:CHERRY-MX-4P
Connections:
- net N$186: now also S81AG$1.PIN-2
- net N$263: now also S81AG$1.PIN-1
- net N$94: no longer S74B.PIN-1
- net N$97: no longer S74B.PIN-2
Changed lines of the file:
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@@
 <part name="2D1" library="detali2" deviceset="74*138" device="N" technology="AC" value="74HC138N"/>
 <part name="JA67B" library="detali" deviceset="SJ" device=""/>
-<part name="S74B" library="cherrymx" deviceset="CHERRY-MX" device="" value="Enter"/>
 <part name="S87" library="cherrymx" deviceset="CHERRY-MX-4P" device="" value="FN2"/>
 <part name="2D2" library="detali2" deviceset="74*04" device="N" technology="ALS" value="74HC04N"/>
@@
 <part name="R7" library="rcl" deviceset="R-EU_" device="R0805" value="10k"/>
 <part name="J13" library="detali2" deviceset="J" device="" value=""/>
+<part name="S81A" library="cherrymx" deviceset="CHERRY-MX-4P" device="" value="R Shift"/>
 </parts>
 <sheets>
@@
 </instance>
 <instance part="JA67B" gate="1" x="203.2" y="73.66"/>
-<instance part="S74B" gate="G$1" x="187.96" y="40.64" rot="MR0"/>
 <instance part="S87" gate="G$1" x="45.72" y="10.16" rot="MR0"/>
 <instance part="2D2" gate="C" x="154.94" y="254"/>
@@
 <attribute name="NAME" x="175.895" y="74.295" size="1.27" layer="95"/>
 </instance>
+<instance part="S81A" gate="G$1" x="187.96" y="38.1" rot="MR0"/>
 </instances>
 <busses>
@@
 <net name="N$94" class="0">
 <segment>
-<wire x1="195.58" y1="40.64" x2="195.58" y2="50.8" width="0.1524" layer="91"/>
 <pinref part="S74A" gate="G$1" pin="PIN-1"/>
-<wire x1="195.58" y1="50.8" x2="193.04" y2="50.8" width="0.1524" layer="91"/>
 <pinref part="JB74" gate="1" pin="2"/>
-<wire x1="198.12" y1="50.8" x2="195.58" y2="50.8" width="0.1524" layer="91"/>
-<junction x="195.58" y="50.8"/>
-<wire x1="195.58" y1="40.64" x2="193.04" y2="40.64" width="0.1524" layer="91"/>
-<pinref part="S74B" gate="G$1" pin="PIN-1"/>
+<wire x1="198.12" y1="50.8" x2="193.04" y2="50.8" width="0.1524" layer="91"/>
 </segment>
 </net>
 <net name="N$97" class="0">
 <segment>
-<wire x1="180.34" y1="40.64" x2="180.34" y2="50.8" width="0.1524" layer="91"/>
 <pinref part="S74A" gate="G$1" pin="PIN-2"/>
-<wire x1="180.34" y1="50.8" x2="182.88" y2="50.8" width="0.1524" layer="91"/>
 <pinref part="JA74" gate="1" pin="1"/>
-<wire x1="177.8" y1="50.8" x2="180.34" y2="50.8" width="0.1524" layer="91"/>
-<junction x="180.34" y="50.8"/>
-<wire x1="182.88" y1="40.64" x2="180.34" y2="40.64" width="0.1524" layer="91"/>
-<pinref part="S74B" gate="G$1" pin="PIN-2"/>
+<wire x1="177.8" y1="50.8" x2="182.88" y2="50.8" width="0.1524" layer="91"/>
 </segment>
 </net>
@@
 <pinref part="JB81" gate="1" pin="2"/>
 <pinref part="S81" gate="G$1" pin="PIN-2"/>
-<wire x1="177.8" y1="30.48" x2="182.88" y2="30.48" width="0.1524" layer="91"/>
+<wire x1="177.8" y1="30.48" x2="180.34" y2="30.48" width="0.1524" layer="91"/>
+<pinref part="S81A" gate="G$1" pin="PIN-2"/>
+<wire x1="180.34" y1="30.48" x2="182.88" y2="30.48" width="0.1524" layer="91"/>
+<wire x1="182.88" y1="38.1" x2="180.34" y2="38.1" width="0.1524" layer="91"/>
+<wire x1="180.34" y1="38.1" x2="180.34" y2="30.48" width="0.1524" layer="91"/>
 </segment>
 </net>
@@
 <pinref part="S81" gate="G$1" pin="PIN-1"/>
 <pinref part="JA81" gate="1" pin="1"/>
-<wire x1="193.04" y1="30.48" x2="198.12" y2="30.48" width="0.1524" layer="91"/>
-</segment>
-</net>
+<wire x1="193.04" y1="30.48" x2="195.58" y2="30.48" width="0.1524" layer="91"/>
+<pinref part="S81A" gate="G$1" pin="PIN-1"/>
+<wire x1="195.58" y1="30.48" x2="198.12" y2="30.48" width="0.1524" layer="91"/>
+<wire x1="193.04" y1="38.1" x2="195.58" y2="38.1" width="0.1524" layer="91"/>
+<wire x1="195.58" y1="38.1" x2="195.58" y2="30.48" width="0.1524" layer="91"/>
+</segment>
+</net>
